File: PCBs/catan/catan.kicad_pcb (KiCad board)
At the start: 2 copper layers, 95.3 x 110 mm, 69 parts, among them J1 Conn_01x04_Female, J2 Conn_01x06_Male, SW1 SW_MEC_5E, SW10 SW_MEC_5E, SW11 SW_MEC_5E, SW2 SW_MEC_5E, SW3 SW_MEC_5E, SW4 SW_MEC_5E, SW5 SW_MEC_5E, SW6 SW_MEC_5E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

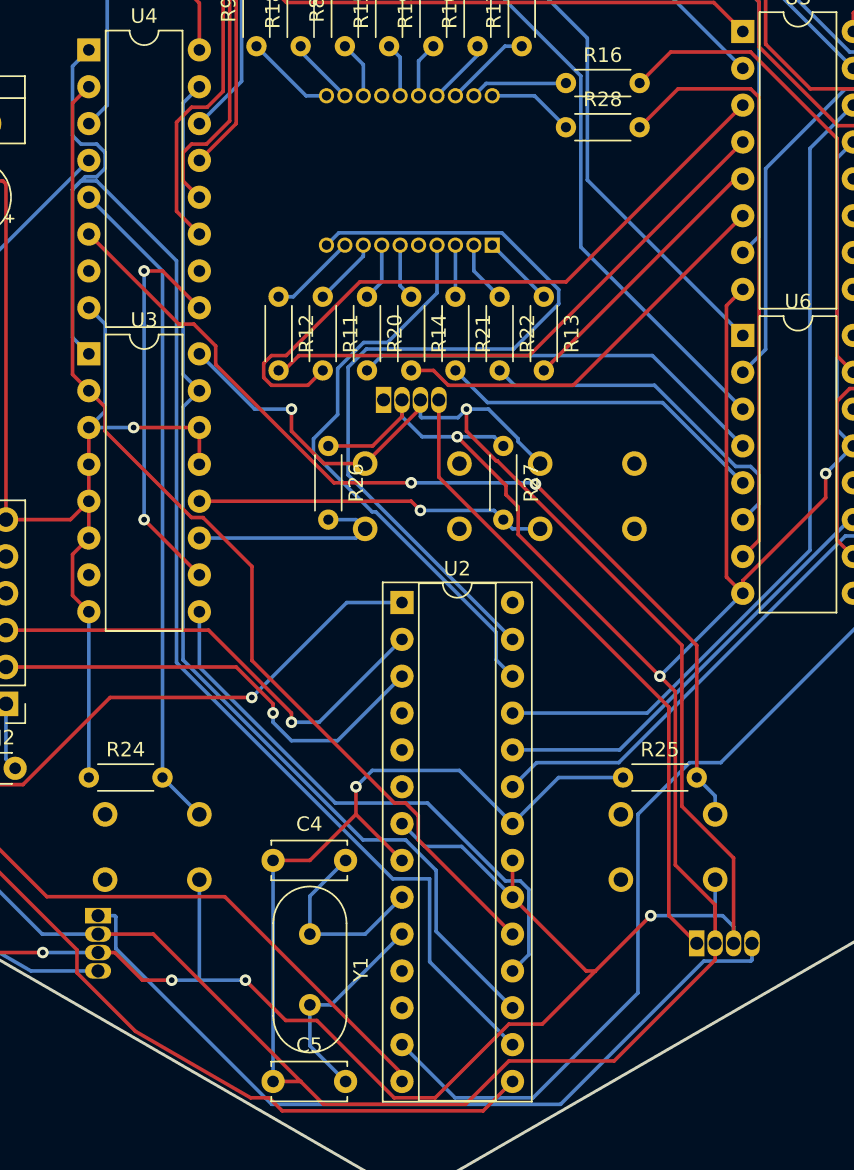
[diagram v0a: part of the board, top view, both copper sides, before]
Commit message: shuffle resistors
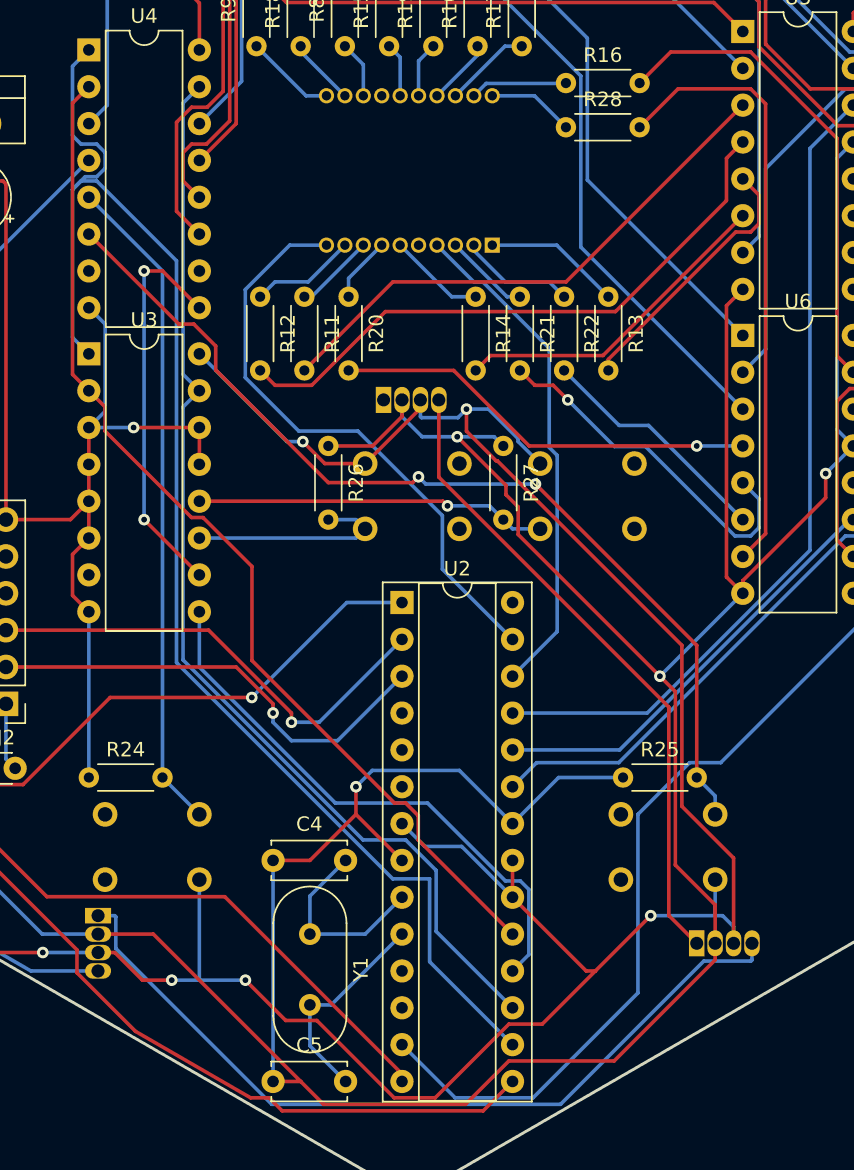
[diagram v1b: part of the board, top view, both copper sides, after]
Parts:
- moved R13 4.44 mm to (138.7, 83.1)
- moved R14 4.44 mm to (129.5, 83.1)
- moved R21 4.44 mm to (132.6, 83.1)
- moved R22 4.44 mm to (135.6, 83.1)
- moved R11 1.27 mm to (117.7, 83.1)
- moved R12 1.27 mm to (114.7, 83.1)
- moved R20 1.27 mm to (120.8, 83.1)
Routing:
- net Net-(DS1-Pad10): track 58.8 -> 41.0 mm
- net Net-(R11-Pad2): track 46.1 -> 37.8 mm
- net Net-(R22-Pad2): track 24.4 -> 16.6 mm
- net Net-(R14-Pad2): track 28.1 -> 22.8 mm
- net Net-(DS1-Pad4): track 40.0 -> 34.8 mm
- net Net-(DS1-Pad1): track 5.03 -> 9.47 mm
- net Net-(R12-Pad2): track 38.5 -> 42.4 mm
- net Net-(DS1-Pad2): track 4.29 -> 7.91 mm
- net Net-(DS1-Pad6): track 3.87 -> 6.68 mm
- net Net-(DS1-Pad3): track 3.56 -> 5.92 mm
- net Net-(R21-Pad2): track 23.0 -> 25.0 mm, vias 0 -> 1
- net Net-(DS1-Pad9): track 6.04 -> 7.31 mm
- net Net-(C2-Pad1): track 507.0 -> 506.1 mm
- net Net-(DS1-Pad8): track 4.71 -> 5.54 mm
- net Net-(R25-Pad2): track 66.6 -> 67.1 mm
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
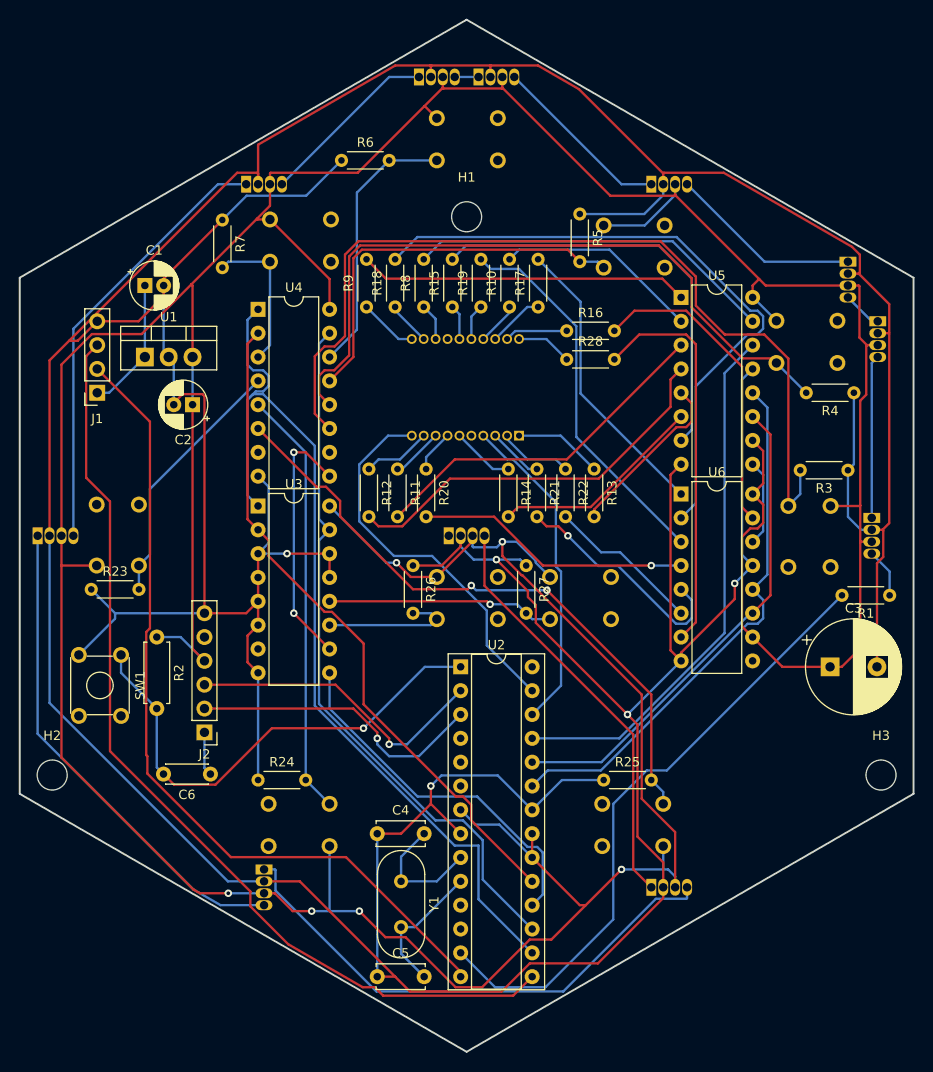
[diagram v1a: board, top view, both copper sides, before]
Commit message: cleaning some traces
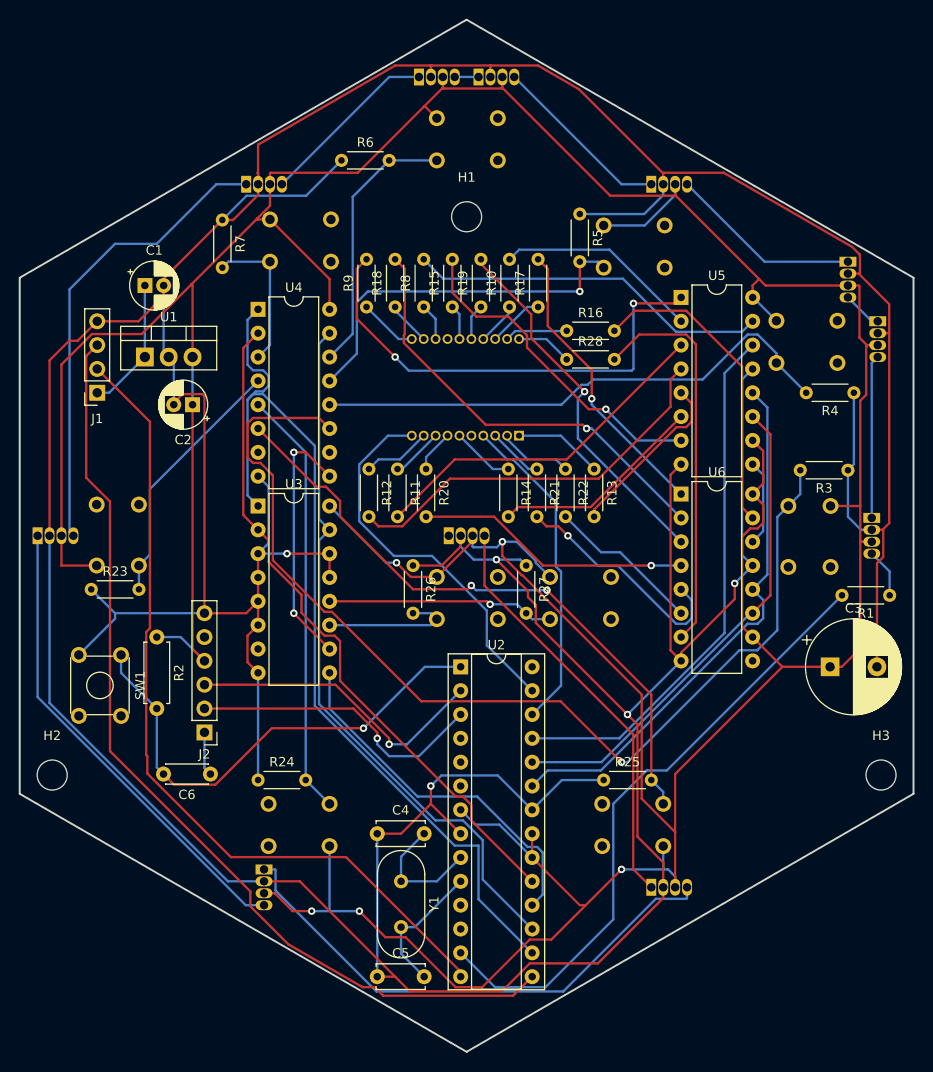
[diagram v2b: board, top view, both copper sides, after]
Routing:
- net Net-(C2-Pad1): track 506.1 -> 480.5 mm, vias 6 -> 5
- net Net-(R18-Pad2): track 69.4 -> 46.6 mm, vias 0 -> 1
- net GND: track 634.1 -> 612.7 mm
- net Net-(R4-Pad2): track 75.7 -> 57.1 mm
- net Net-(R3-Pad2): track 96.0 -> 112.2 mm, vias 0 -> 1
- net Net-(R9-Pad2): track 35.2 -> 50.9 mm, vias 0 -> 2
- net Net-(R15-Pad2): track 45.3 -> 35.2 mm, vias 0 -> 1
- net Net-(D7-Pad1): track 46.9 -> 49.9 mm
- net Net-(R5-Pad2): track 42.0 -> 39.8 mm, vias 0 -> 1
- net Net-(D8-Pad1): track 52.6 -> 50.5 mm
- net Net-(R19-Pad2): track 40.7 -> 39.5 mm, vias 0 -> 1
- net Net-(R8-Pad2): track 39.4 -> 38.7 mm
- net Net-(U2-Pad19): track 72.4 -> 72.9 mm
- net Net-(R17-Pad2): vias 0 -> 1

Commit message: go back to original catan layout
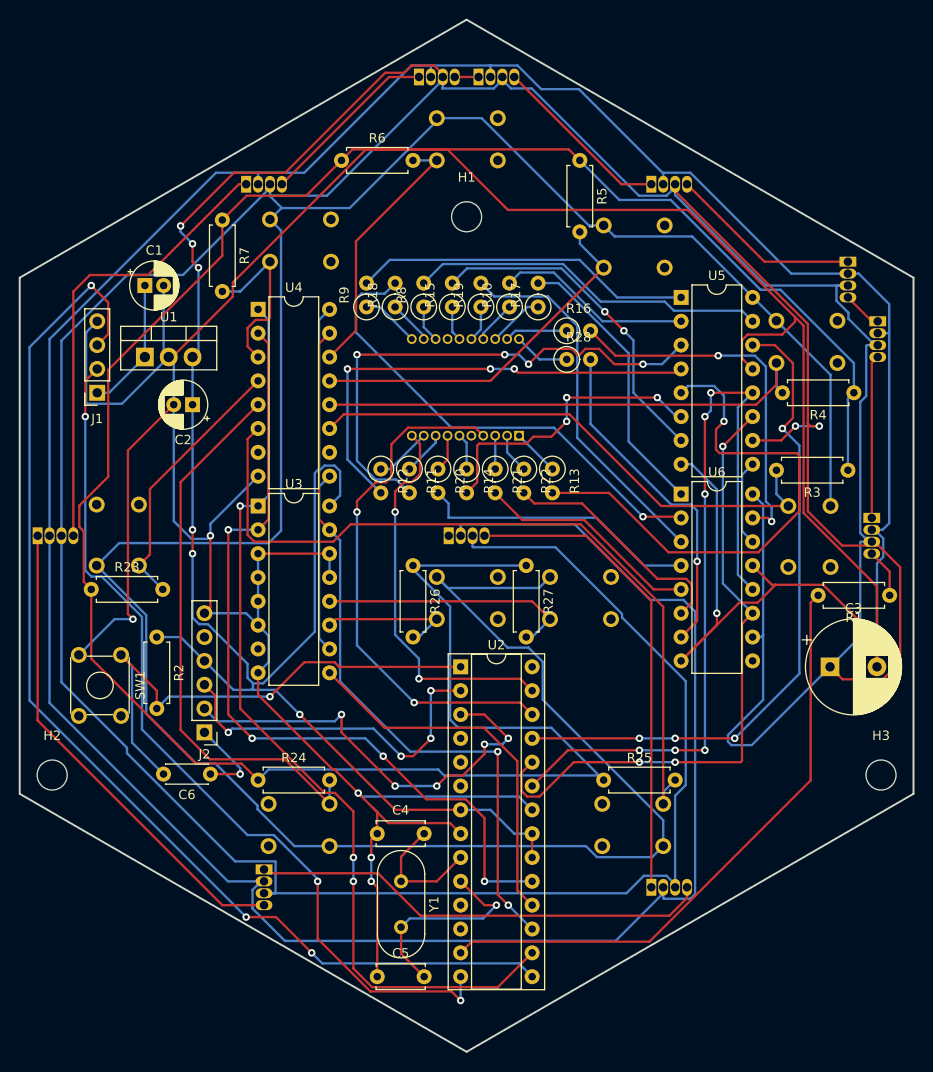
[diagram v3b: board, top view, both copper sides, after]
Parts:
- R1, R23, R24, R25, R26, R27, R3, R4, R5, R6, R7: footprint Resistor_THT:R_Axial_DIN0204_L3.6mm_D1.6mm_P5.08mm_Horizontal -> Resistor_THT:R_Axial_DIN0207_L6.3mm_D2.5mm_P7.62mm_Horizontal
- R10, R11, R12, R13, R14, R15, R16, R17, R18, R19, R20, R21, R22, R28, R8, R9: footprint Resistor_THT:R_Axial_DIN0204_L3.6mm_D1.6mm_P5.08mm_Horizontal -> Resistor_THT:R_Axial_DIN0207_L6.3mm_D2.5mm_P2.54mm_Vertical
- moved R5 5.72 mm to (137.2, 50.2)
- moved R13 4.44 mm to (134.2, 83.1)
- moved R14 4.44 mm to (125.1, 83.1)
- moved R21 4.44 mm to (128.1, 83.1)
- moved R22 4.44 mm to (131.2, 83.1)
- moved R11 1.27 mm to (119.0, 83.1)
- moved R12 1.27 mm to (116.0, 83.1)
- moved R20 1.27 mm to (122.0, 83.1)
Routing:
- net Net-(C2-Pad1): track 480.5 -> 925.3 mm, vias 5 -> 8
- net GND: track 612.7 -> 991.7 mm, vias 5 -> 6
- net Net-(R3-Pad2): track 112.2 -> 57.9 mm, vias 1 -> 0
- net Net-(R13-Pad2): track 19.1 -> 57.2 mm, vias 0 -> 1
- net Net-(U2-Pad23): track 57.8 -> 85.1 mm, vias 0 -> 6
- net Net-(DS1-Pad4): track 34.8 -> 56.2 mm, vias 0 -> 2
- net Net-(J1-Pad3): track 101.7 -> 120.3 mm, vias 0 -> 3
- net Net-(R11-Pad2): track 37.8 -> 56.0 mm, vias 0 -> 4
- net Net-(R25-Pad2): track 67.1 -> 84.9 mm, vias 2 -> 0
- net Net-(U2-Pad24): track 52.6 -> 68.6 mm, vias 0 -> 3
- net Net-(U2-Pad19): track 72.9 -> 88.4 mm, vias 0 -> 4
- net Net-(R9-Pad2): track 50.9 -> 36.2 mm, vias 2 -> 0
- net Net-(J2-Pad2): track 32.0 -> 46.4 mm, vias 1 -> 5
- net Net-(R24-Pad2): track 45.7 -> 59.8 mm
- net Net-(U2-Pad25): track 57.1 -> 70.7 mm, vias 0 -> 4
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
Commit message: replace resistor footprints and redo traces
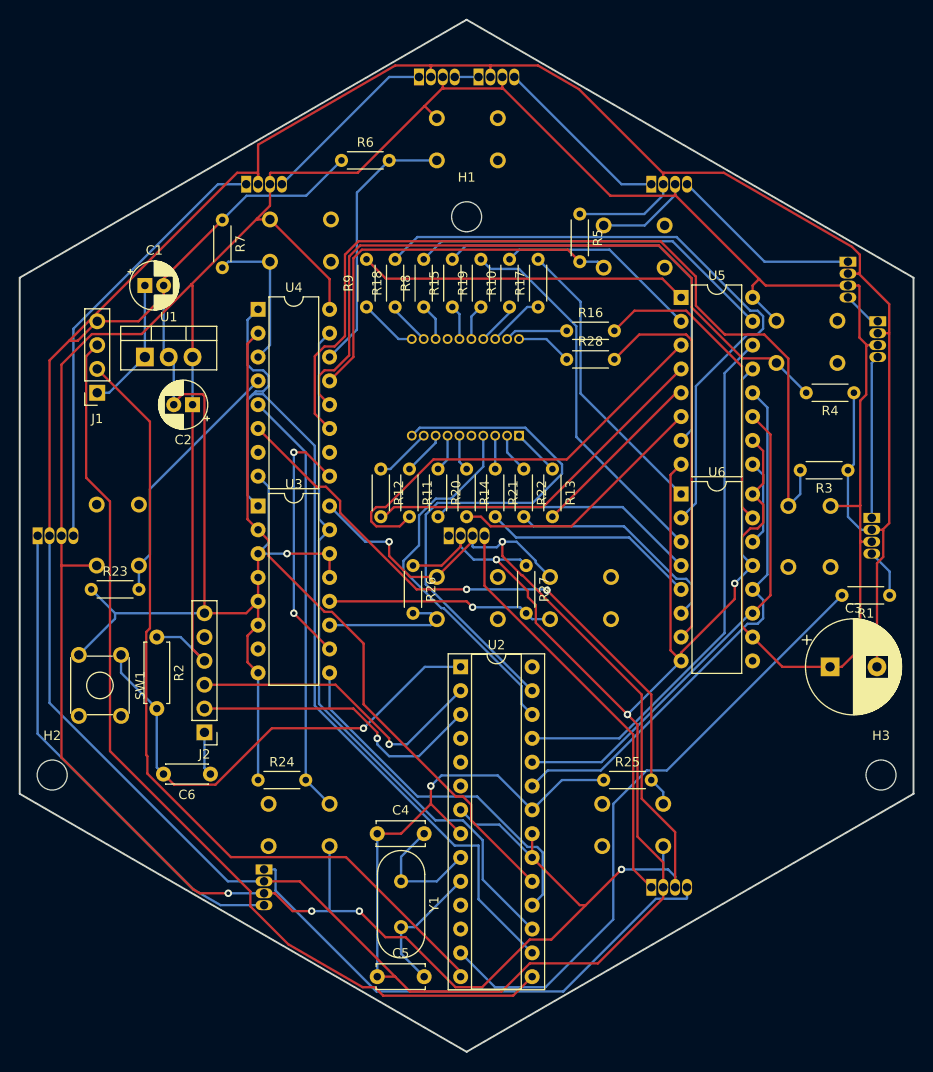
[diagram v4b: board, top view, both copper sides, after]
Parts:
- R1, R23, R24, R25, R26, R27, R3, R4, R5, R6, R7: footprint Resistor_THT:R_Axial_DIN0207_L6.3mm_D2.5mm_P7.62mm_Horizontal -> Resistor_THT:R_Axial_DIN0204_L3.6mm_D1.6mm_P5.08mm_Horizontal
- R10, R11, R12, R13, R14, R15, R16, R17, R18, R19, R20, R21, R22, R28, R8, R9: footprint Resistor_THT:R_Axial_DIN0207_L6.3mm_D2.5mm_P2.54mm_Vertical -> Resistor_THT:R_Axial_DIN0204_L3.6mm_D1.6mm_P5.08mm_Horizontal
- moved R5 5.72 mm to (137.2, 55.9)
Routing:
- net Net-(C2-Pad1): track 925.3 -> 507.0 mm, vias 8 -> 6
- net GND: track 991.7 -> 634.1 mm, vias 6 -> 5
- net Net-(R3-Pad2): track 57.9 -> 96.0 mm
- net Net-(R13-Pad2): track 57.2 -> 19.2 mm, vias 1 -> 0
- net Net-(U2-Pad23): track 85.1 -> 57.8 mm, vias 6 -> 0
- net Net-(R4-Pad2): track 54.3 -> 75.7 mm
- net Net-(J1-Pad3): track 120.3 -> 101.7 mm, vias 3 -> 0
- net Net-(R25-Pad2): track 84.9 -> 66.6 mm, vias 0 -> 2
- net Net-(R18-Pad2): track 51.3 -> 69.4 mm, vias 1 -> 0
- net Net-(DS1-Pad10): track 41.5 -> 58.8 mm, vias 2 -> 0
- net Net-(DS1-Pad4): track 56.2 -> 40.0 mm, vias 2 -> 0
- net Net-(U2-Pad19): track 88.4 -> 72.4 mm, vias 4 -> 0
- net Net-(U2-Pad24): track 68.6 -> 52.6 mm, vias 3 -> 0
- net Net-(J2-Pad2): track 46.4 -> 32.0 mm, vias 5 -> 1
- net Net-(R24-Pad2): track 59.8 -> 45.7 mm
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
